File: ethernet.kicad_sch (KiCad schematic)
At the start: 76 parts, among them IC2 TPS2378DDA, J2 5-2337992-8, U6 KSZ9031RNXCA, Y1 ABM8G-25.000MHZ-18-D2Y-T

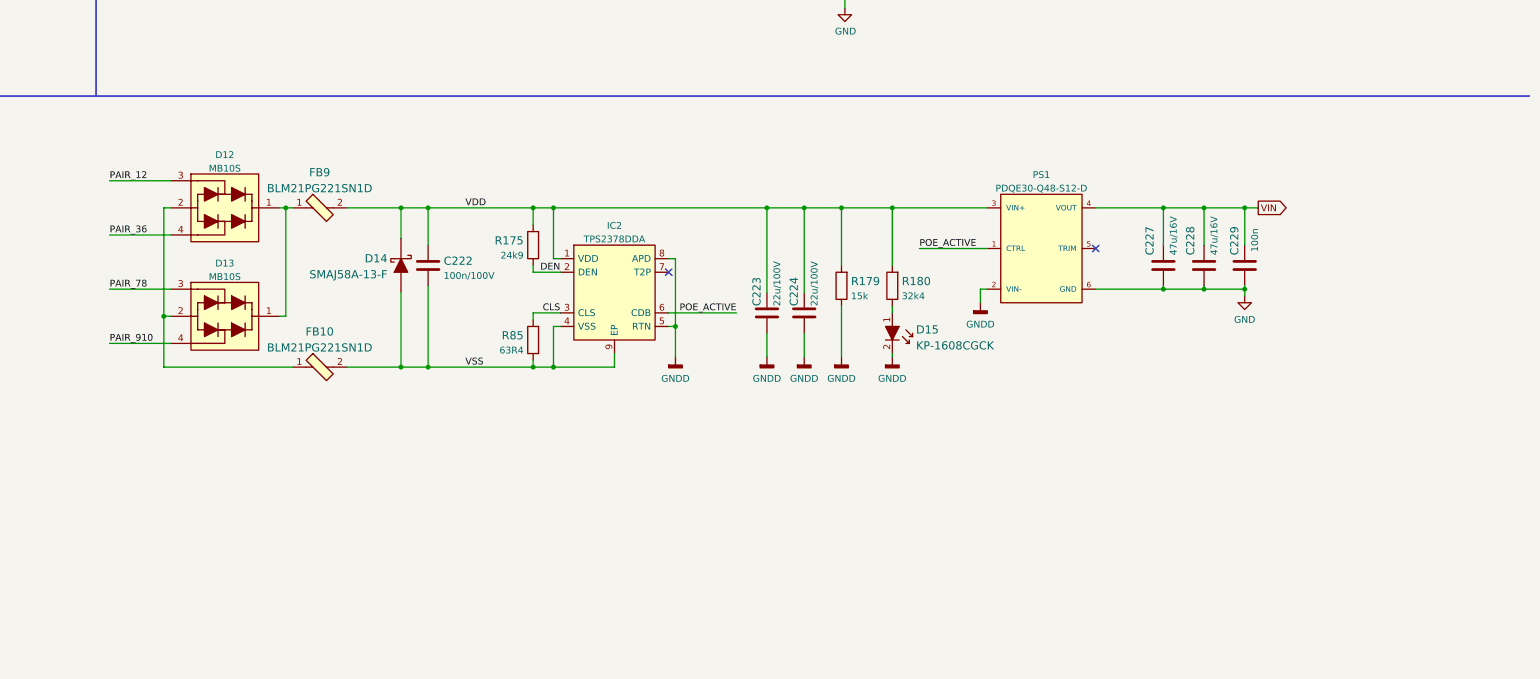
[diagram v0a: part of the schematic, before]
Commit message: Change PoE controller to TPS2373-4RGWR and update placement on PCB
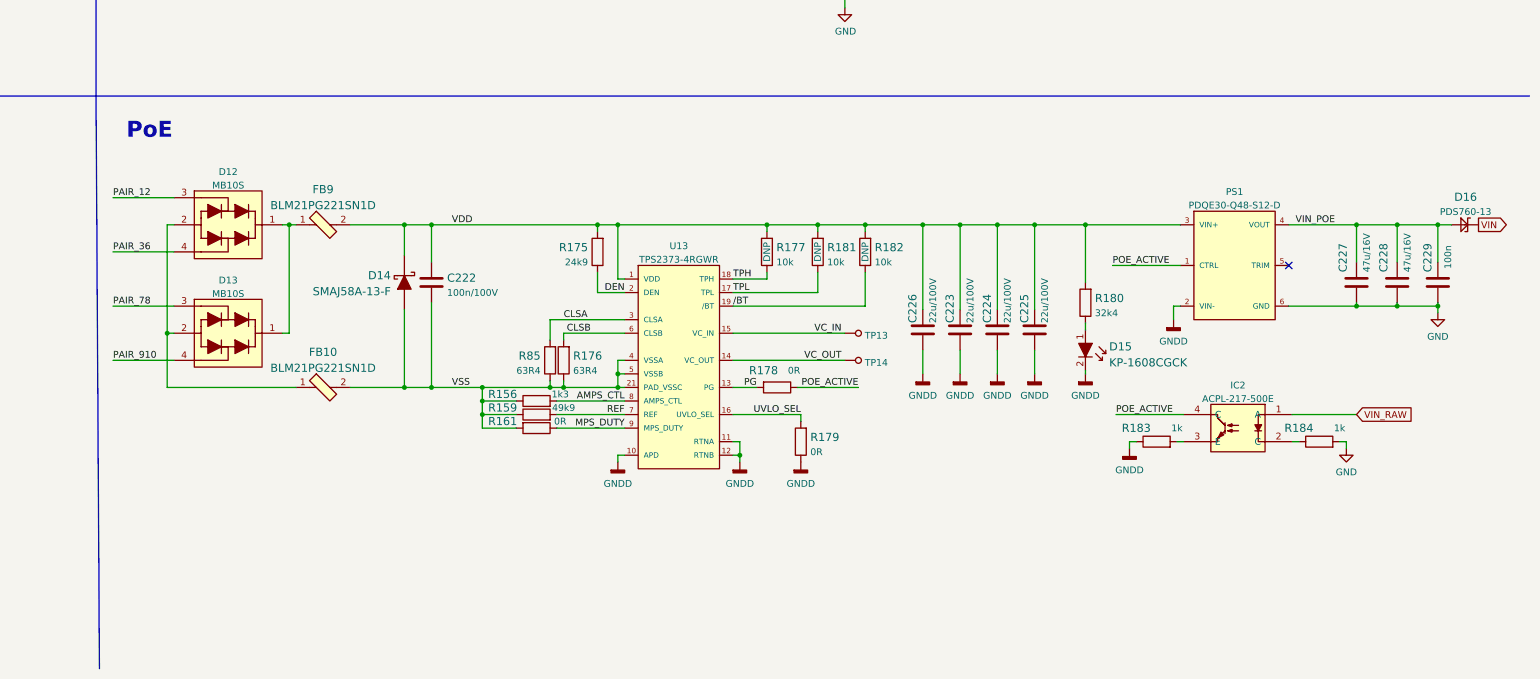
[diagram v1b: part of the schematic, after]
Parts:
- removed IC2: TPS2378DDA, antmicro-footprints:SOIC127P600X170-9N, symbol antmicroPMICPowerDistributionSwitchesLoadDrivers:TPS2378DDA
- removed R179: R_15k_0603, antmicro-footprints:0603-res, symbol antmicroResistors0603:R_15k_0603
- added C225, C226: C_22u_2220_100V, antmicro-footprints:2220-cap, symbol antmicroCapacitorsmisc:C_22u_2220_100V
- added D16: PDS760-13, data-center-dram-tester-footprints:PDS760-13, symbol data-center-dram-tester:PDS760-13
- added IC2: ACPL-217-500E, antmicro-footprints:SOIC127P700X242-4N, symbol antmicroOptoisolatorsLogicOutput:ACPL-217-500E
- added R156: R_1k3_0603, antmicro-footprints:0603-res, symbol antmicroResistors0603:R_1k3_0603
- added R159: R_49k9_0402, antmicro-footprints:0402-res, symbol antmicroResistors0402:R_49k9_0402
- added R161, R178, R179: R_0R_0402, antmicro-footprints:0603-res, symbol antmicroResistors0603:R_0R_0603
- added R176: R_63R4_0603, antmicro-footprints:0603-res, symbol antmicroResistors0603:R_63R4_0603
- added R177, R181, R182: R_10k_0402, antmicro-footprints:0402-res, symbol antmicroResistors0402:R_10k_0402
- added R183, R184: R_1k_0603, antmicro-footprints:0603-res, symbol antmicroResistors0603:R_1k_0603
- added TP13, TP14: TP_SMD1MM, data-center-dram-tester-footprints:Testpoint_smd_1mm, symbol data-center-dram-tester:TP_SMD1MM
- added U13: TPS2373-4RGWR, antmicro-footprints:QFN65P500X500X100-21N, symbol antmicroPMICPowerDistributionSwitchesLoadDrivers:TPS2373-4RGWR
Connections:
- net DEN: now also U13.2 (DEN)
- net GND: now also R184.2
- net GNDD: now also C225.2, C226.2, R179.1, R183.1, U13.10 (APD), U13.11 (RTNA), U13.12 (RTNB)
- net POE_ACTIVE: now also IC2.4 (C), R178.1
- net VDD: now also C225.1, C226.1, R177.2, R181.2, R182.2, U13.1 (VDD)
- net VIN: now also D16.C; no longer C227.1, C228.1, C229.1, PS1.4 (VOUT)
- net VSS: now also R156.1, R159.1, R161.2, R176.1, U13.21 (PAD_VSSC), U13.4 (VSSA), U13.5 (VSSB)
- net CLS renamed CLSA
- net CLSA: now also U13.3 (CLSA)
- new net: IC2.2 (C), R184.1
- new net: IC2.3 (E), R183.2
- new net AMPS_CTL: R156.2, U13.8 (AMPS_CTL)
- new net CLSB: R176.2, U13.6 (CLSB)
- new net MPS_DUTY: R161.1, U13.9 (MPS_DUTY)
- new net PG: R178.2, U13.13 (PG)
- new net REF: R159.2, U13.7 (REF)
- new net TPH: R177.1, U13.18 (TPH)
- new net TPL: R181.1, U13.17 (TPL)
- new net UVLO_SEL: R179.2, U13.16 (UVLO_SEL)
- new net VC_IN: TP13.1, U13.15 (VC_IN)
- new net VC_OUT: TP14.1, U13.14 (VC_OUT)
- new net VIN_POE: C227.1, C228.1, C229.1, D16.A, PS1.4 (VOUT)
- new net VIN_RAW: IC2.1 (A)
- new net /BT: R182.1, U13.19 (/BT)
- no-connect marks 3 -> 2
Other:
- note added: "PoE"
- moved on the sheet: C222, C223, C224, C227, C228, C229, D12, D13, D14, D15, FB10, FB9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

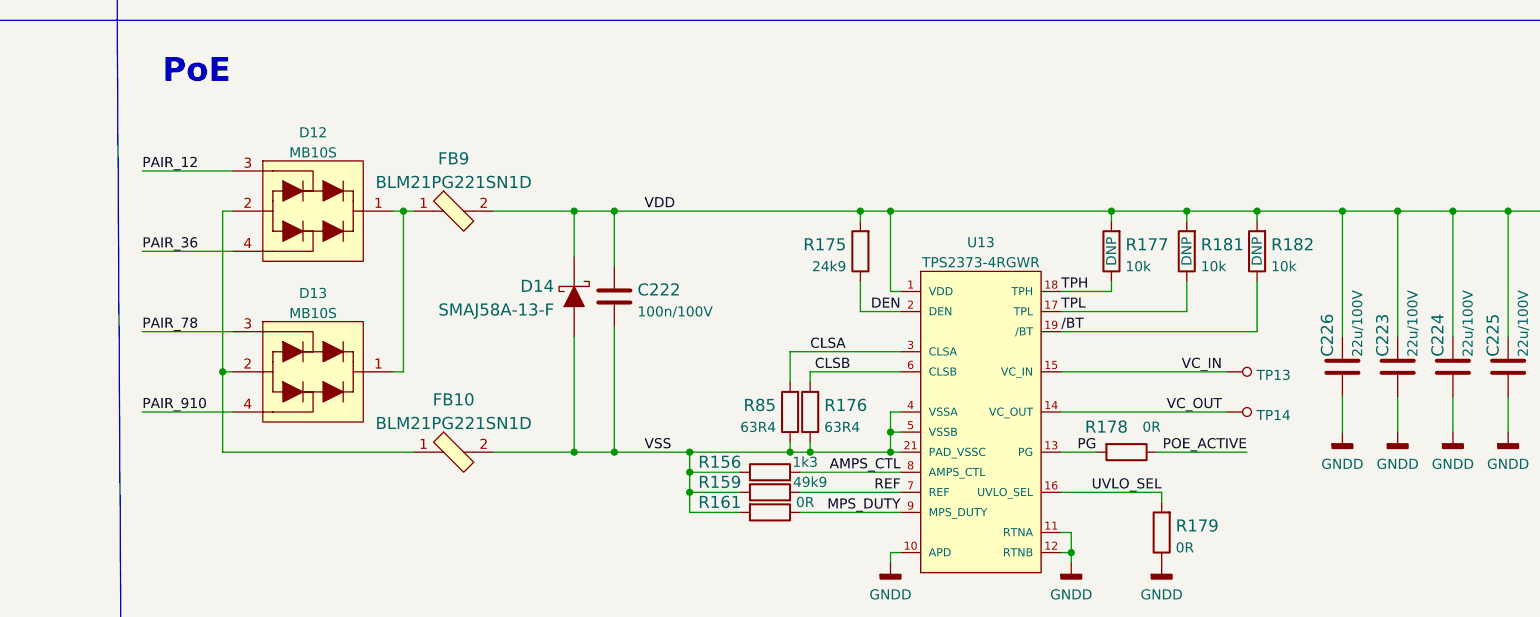
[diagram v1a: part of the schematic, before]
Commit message: Finish layout with new PoE controller. DRC and silks clearing
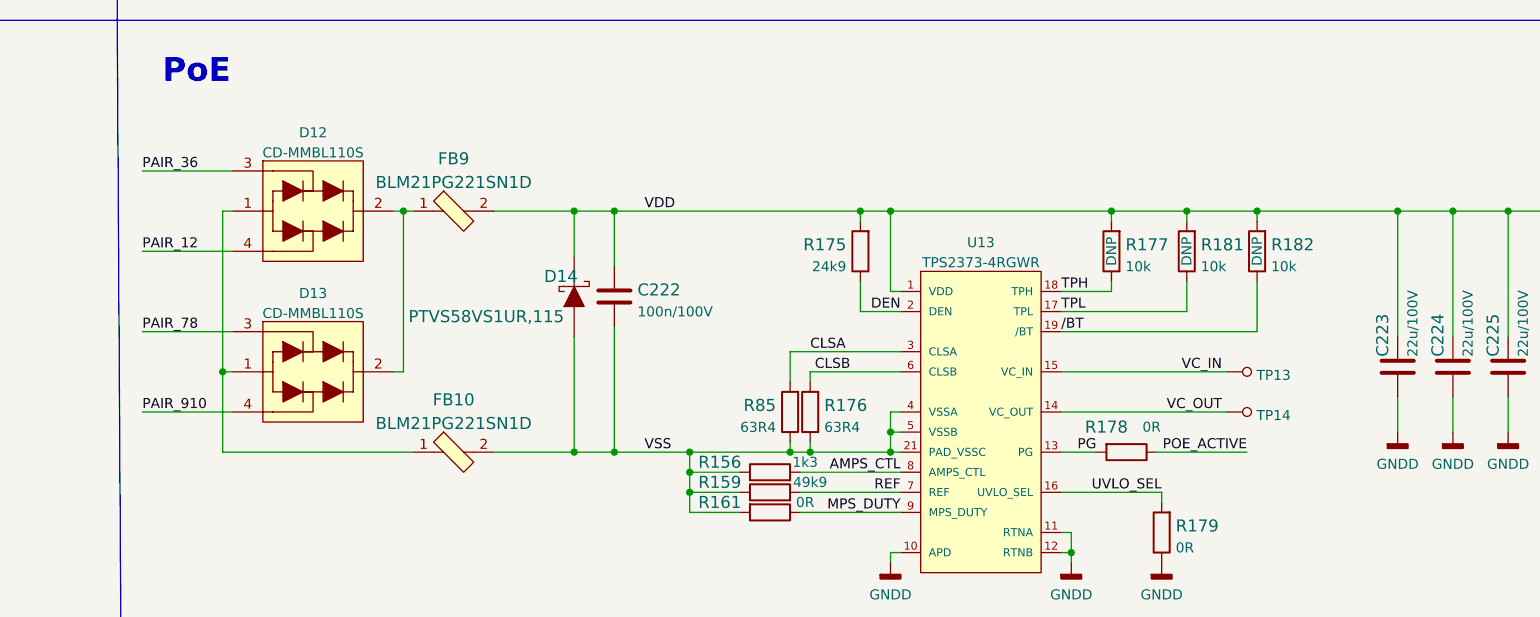
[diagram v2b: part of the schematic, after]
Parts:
- removed C226: C_22u_2220_100V, antmicro-footprints:2220-cap, symbol antmicroCapacitorsmisc:C_22u_2220_100V
- removed D12, D13: MB10S, antmicro-footprints:MB10S, symbol antmicroTVSDiodes:MB10S
- removed D14: SMAJ58A-13-F, antmicro-footprints:DO-214AC, symbol antmicroDiodesRectifiersSingle:SMAJ58A-13-F
- added D12, D13: CD-MMBL110S, antmicro-footprints:DFN3538, symbol antmicroTVSDiodes:CD-MMBL110S
- added D14: PTVS58VS1UR,115, antmicro-footprints:SOD-123F, symbol antmicroDiodesRectifiersSingle:PTVS58VS1UR,115
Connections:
- net PAIR_12: now also D12.4
- net PAIR_36: now also D12.3
- net PAIR_78: now also D13.3
- net PAIR_910: now also D13.4
- net VDD: now also D14.K
- net VSS: now also D14.A
- net at FB9.1: now also D12.2, D13.2
- net at FB10.1: now also D12.1, D13.1

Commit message: Loclib
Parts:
- C221: footprint antmicro-footprints:0402-cap -> data-center-dram-tester-footprints:0402-cap; symbol antmicroCapacitors0402:C_10n_0402 -> data-center-dram-tester:C_10n_0402
- C222: footprint antmicro-footprints:0805-cap -> data-center-dram-tester-footprints:0805-cap; symbol antmicroCapacitorsmisc:C_100n_0805_100V -> data-center-dram-tester:C_100n_0805_100V
- C223, C224, C225: footprint antmicro-footprints:2220-cap -> data-center-dram-tester-footprints:2220-cap; symbol antmicroCapacitorsmisc:C_22u_2220_100V -> data-center-dram-tester:C_22u_2220_100V
- C227, C228: footprint antmicro-footprints:1206-cap -> data-center-dram-tester-footprints:1206-cap; symbol antmicroCapacitorsmisc:C_47u_16V_1206 -> data-center-dram-tester:C_47u_16V_1206
- D12, D13: footprint antmicro-footprints:DFN3538 -> data-center-dram-tester-footprints:DFN3538; symbol antmicroTVSDiodes:CD-MMBL110S -> data-center-dram-tester:CD-MMBL110S
- D14: footprint antmicro-footprints:SOD-123F -> data-center-dram-tester-footprints:SOD-123F; symbol antmicroDiodesRectifiersSingle:PTVS58VS1UR,115 -> data-center-dram-tester:PTVS58VS1UR,115
- D15: footprint antmicro-footprints:LED_0603 -> data-center-dram-tester-footprints:LED_0603; symbol antmicroLEDIndicationDiscrete:KP-1608CGCK -> data-center-dram-tester:KP-1608CGCK
- FB10, FB9: footprint antmicro-footprints:0805-res -> data-center-dram-tester-footprints:0805-res; symbol antmicroFerriteBeadsandChips:BLM21PG221SN1D -> data-center-dram-tester:BLM21PG221SN1D
- IC2: footprint antmicro-footprints:SOIC127P700X242-4N -> data-center-dram-tester-footprints:SOIC127P700X242-4N; symbol antmicroOptoisolatorsLogicOutput:ACPL-217-500E -> data-center-dram-tester:ACPL-217-500E
- J2: footprint antmicro-footprints:5-2337992-8 -> data-center-dram-tester-footprints:5-2337992-8; symbol antmicroModularConnectorsJacksWithMagnetics:5-2337992-8 -> data-center-dram-tester:5-2337992-8
- PS1: footprint antmicro-footprints:PDQE30-Q48 -> data-center-dram-tester-footprints:PDQE30-Q48; symbol antmicroDCDCConverters:PDQE30-Q48-S12-D -> data-center-dram-tester:PDQE30-Q48-S12-D
- R156: footprint antmicro-footprints:0603-res -> data-center-dram-tester-footprints:0603-res; symbol antmicroResistors0603:R_1k3_0603 -> data-center-dram-tester:R_1k3_0603
- R159: footprint antmicro-footprints:0402-res -> data-center-dram-tester-footprints:0402-res; symbol antmicroResistors0402:R_49k9_0402 -> data-center-dram-tester:R_49k9_0402
- R161, R178, R179: footprint antmicro-footprints:0603-res -> data-center-dram-tester-footprints:0603-res; symbol antmicroResistors0603:R_0R_0603 -> data-center-dram-tester:R_0R_0603
- R175: footprint antmicro-footprints:0402-res -> data-center-dram-tester-footprints:0402-res; symbol antmicroResistors0402:R_24k9_0402 -> data-center-dram-tester:R_24k9_0402
- R176, R85: footprint antmicro-footprints:0603-res -> data-center-dram-tester-footprints:0603-res; symbol antmicroResistors0603:R_63R4_0603 -> data-center-dram-tester:R_63R4_0603
- R177, R181, R182: footprint antmicro-footprints:0402-res -> data-center-dram-tester-footprints:0402-res; symbol antmicroResistors0402:R_10k_0402 -> data-center-dram-tester:R_10k_0402
- R180: footprint antmicro-footprints:0402-res -> data-center-dram-tester-footprints:0402-res; symbol antmicroResistors0402:R_32k4_0402 -> data-center-dram-tester:R_32k4_0402
- R183, R184: footprint antmicro-footprints:0603-res -> data-center-dram-tester-footprints:0603-res; symbol antmicroResistors0603:R_1k_0603 -> data-center-dram-tester:R_1k_0603
- U13: footprint antmicro-footprints:QFN65P500X500X100-21N -> data-center-dram-tester-footprints:QFN65P500X500X100-21N; symbol antmicroPMICPowerDistributionSwitchesLoadDrivers:TPS2373-4RGWR -> data-center-dram-tester:TPS2373-4RGWR
